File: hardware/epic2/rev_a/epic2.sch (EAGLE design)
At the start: 32 parts, among them J1 PINHD-1X10/0.050, J2 PINHD-1X10/0.050, J3 PINHD-1X10/0.050, U2 FM25LBTDFN-8, U3 CC2538, X1 EPSON-FA-128, X2 FC-12M32.7680KA-A3

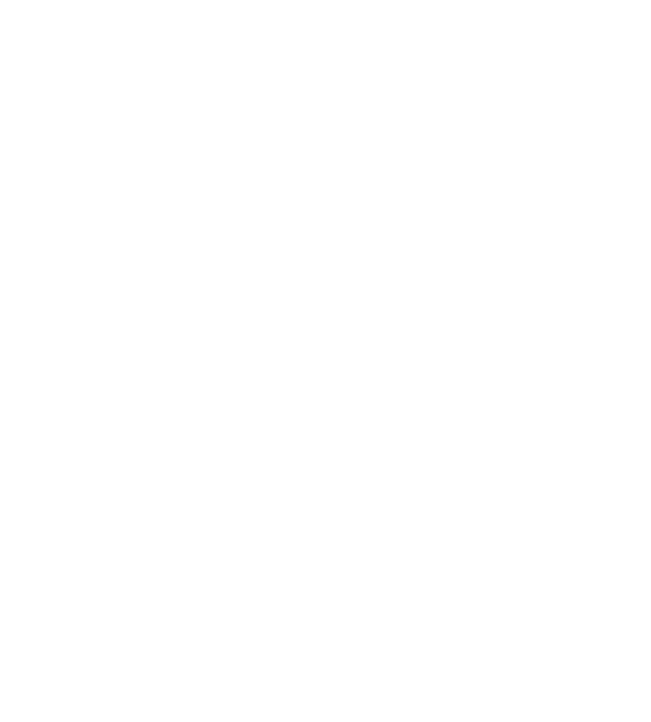
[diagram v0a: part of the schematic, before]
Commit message: new headers
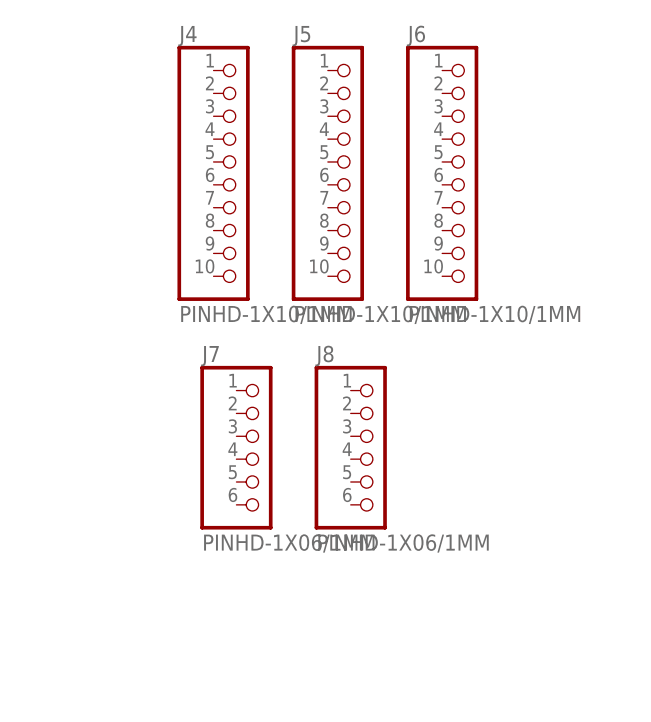
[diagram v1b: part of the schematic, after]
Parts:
- added J4, J5, J6: PINHD-1X10/1MM, headers:PINHD-1X10/1MM
- added J7, J8: PINHD-1X06/1MM, headers:PINHD-1X06/1MM
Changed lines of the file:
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@@
 <part name="C17" library="passives" deviceset="CAPACITOR" device="" value="22pF"/>
 <part name="GND1" library="supply1" deviceset="GND" device=""/>
+<part name="J4" library="headers" deviceset="PINHD-1X10/1MM" device=""/>
+<part name="J5" library="headers" deviceset="PINHD-1X10/1MM" device=""/>
+<part name="J6" library="headers" deviceset="PINHD-1X10/1MM" device=""/>
+<part name="J7" library="headers" deviceset="PINHD-1X06/1MM" device=""/>
+<part name="J8" library="headers" deviceset="PINHD-1X06/1MM" device=""/>
 </parts>
 <sheets>
@@
 <instance part="C17" gate="G$1" x="104.14" y="86.36" rot="R90"/>
 <instance part="GND1" gate="1" x="116.84" y="88.9"/>
+<instance part="J4" gate="G$1" x="264.16" y="170.18"/>
+<instance part="J5" gate="G$1" x="276.86" y="170.18"/>
+<instance part="J6" gate="G$1" x="289.56" y="170.18"/>
+<instance part="J7" gate="G$1" x="266.7" y="137.16"/>
+<instance part="J8" gate="G$1" x="279.4" y="137.16"/>
 </instances>
 <busses>

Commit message: dummy routing for epic2
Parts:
- removed J1, J2, J3: PINHD-1X10/0.050, headers:PINHD-1X10/0.050
- removed J5: PINHD-1X10/1MM, headers:PINHD-1X10/1MM
- removed R5: 4.7k, passives:RESISTOR
- added C18: 10nF, passives:CAPACITOR
- added D1: SML-LX0404SIUPGUSB, leds:SML-LX0404SIUPGUSB
- added R2: 1k, passives:RESISTOR
- added U1: RV-4162-C7, chips:RV-4162-C7
- R3, R4: value 4.7k -> 1k
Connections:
- removed net A3: U3.PA3/ROM-SSI-SEL
- removed net A4: U3.PA4/ROM-SSI-RX
- removed net A5: U3.PA5/ROM-SSI-TX
- removed net A6: U3.PA6
- removed net A7: U3.PA7
- removed net DS2411: U3.PB0
- removed net MISO: U2.SO
- removed net MOSI: U2.SI
- removed net SCK: U2.SCK
- new net !RTC_INT: U1.!INT, U3.PB6/JTAG-TDI
- new net ADC3: J6.4, U3.PA3/ROM-SSI-SEL
- new net ADC4: J6.5, U3.PA4/ROM-SSI-RX
- new net ADC5: J6.6, U3.PA5/ROM-SSI-TX
- new net ADC6: J6.7, U3.PA6
- new net ADC7: J6.8, U3.PA7
- new net B1: J4.10, U3.PB1
- new net B2: J4.9, U3.PB2
- new net B3: J4.8, U3.PB3
- new net B4: J4.7, U3.PB4
- new net DGND_USB: J7.1, U3.DGND_USB
- new net DVDD_USB: J7.4, U3.DVDD_USB
- new net I2C_SCL: J8.2, U1.SCL, U3.PC5
- new net I2C_SDA: J8.3, U1.SDA, U3.PC4
- new net LED_BLUE: R4.2, U3.PC7
- new net LED_GREEN: R3.2, U3.PC6
- new net LED_RED: R2.2, U3.PB0
- new net N$11: D1.G, R3.1
- new net N$12: D1.B, R4.1
- new net N$7: D1.R, R2.1
- new net RTC_CLKOUT: U1.CLKOUT, U3.PB5
- new net SPI_MISO: J7.5, U2.SO, U3.PD0
- new net SPI_MOSI: J7.6, U2.SI, U3.PD1
- new net SPI_SCK: J8.1, U2.SCK, U3.PD2
- new net UNUSED1: J4.2
- new net UNUSED2: J4.3
- new net USB_N: J7.3, U3.USB_N
- new net USB_P: J7.2, U3.USB_P
- net !FRAM_CS: now also U3.PD4; no longer R3.1, U3.PB4
- net !FRAM_HOLD: now also U3.PD3; no longer R4.1, U3.PB3
- net !FRAM_WP: now also U3.PD5; no longer R5.1, U3.PB5
- net !RESET: now also J6.9
- net BOOTLOADER_CTRL: now also J6.3
- net BOOTLOADER_RX: now also J6.1
- net BOOTLOADER_TX: now also J6.2
- net C0: now also J8.6
- net C1: now also J8.5
- net C2: now also J8.4
- net GND: now also C18.2, J6.10, U1.GND
- net TCK: now also J4.5
- net TDO: now also J4.6
- net TMS: now also J4.4
- net VCC: now also C18.1, D1.VDD, J4.1, U1.VCC; no longer R3.2, R4.2, R5.2
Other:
- note added: "I2C address: 0xD0"
- moved on the sheet: C1, C16, C17, C2, C5, J4, J6, J7, J8, R3, R4, U2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

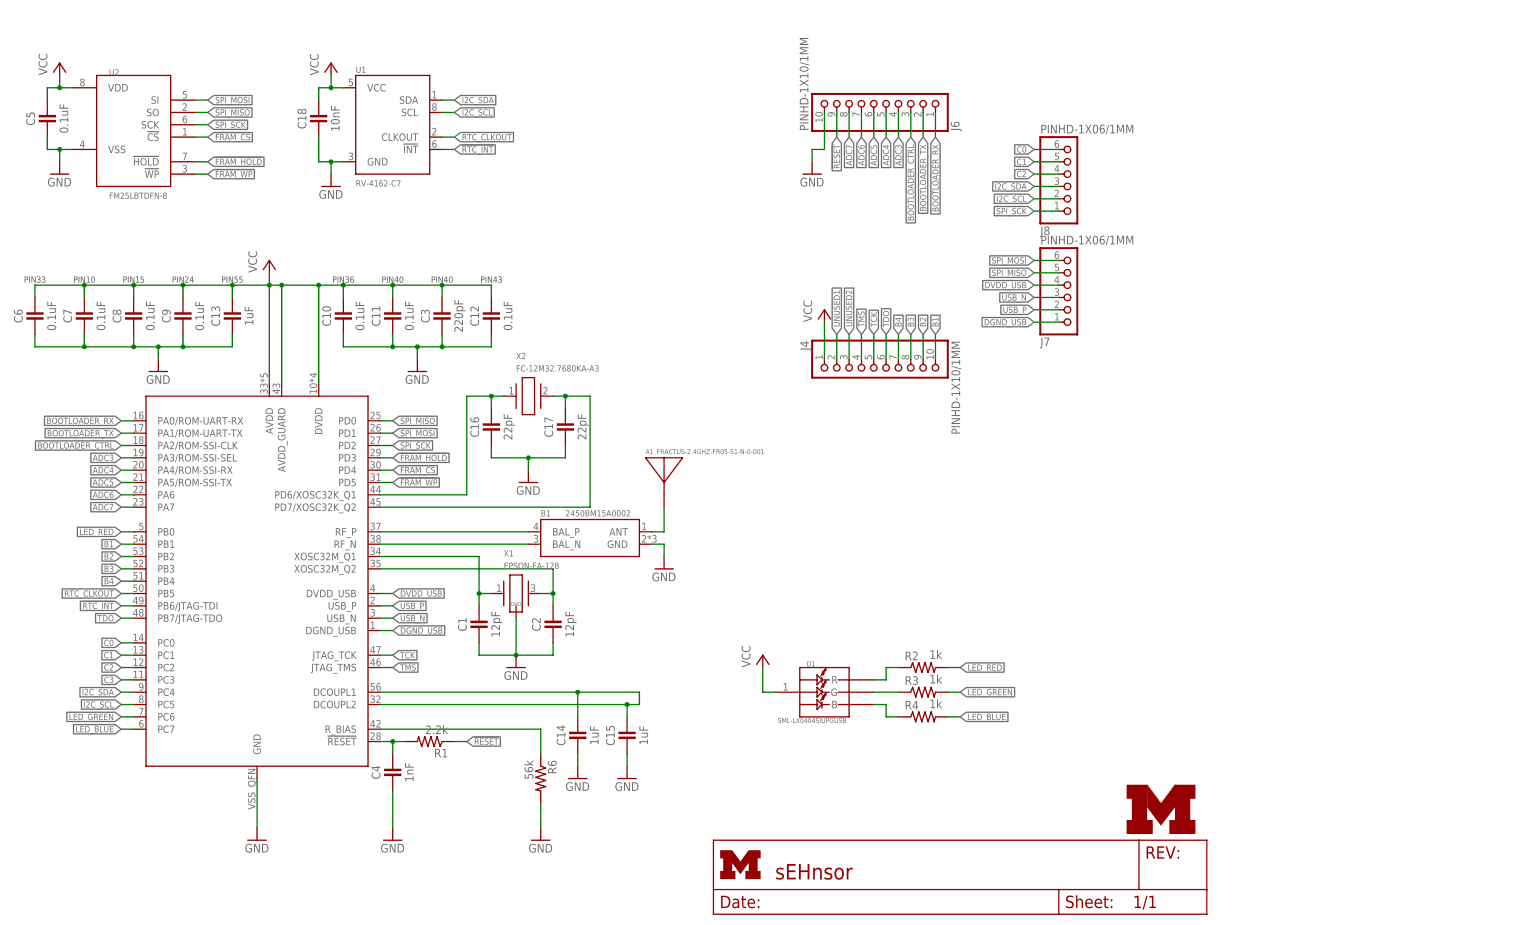
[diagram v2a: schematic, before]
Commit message: rectangular board close to routed
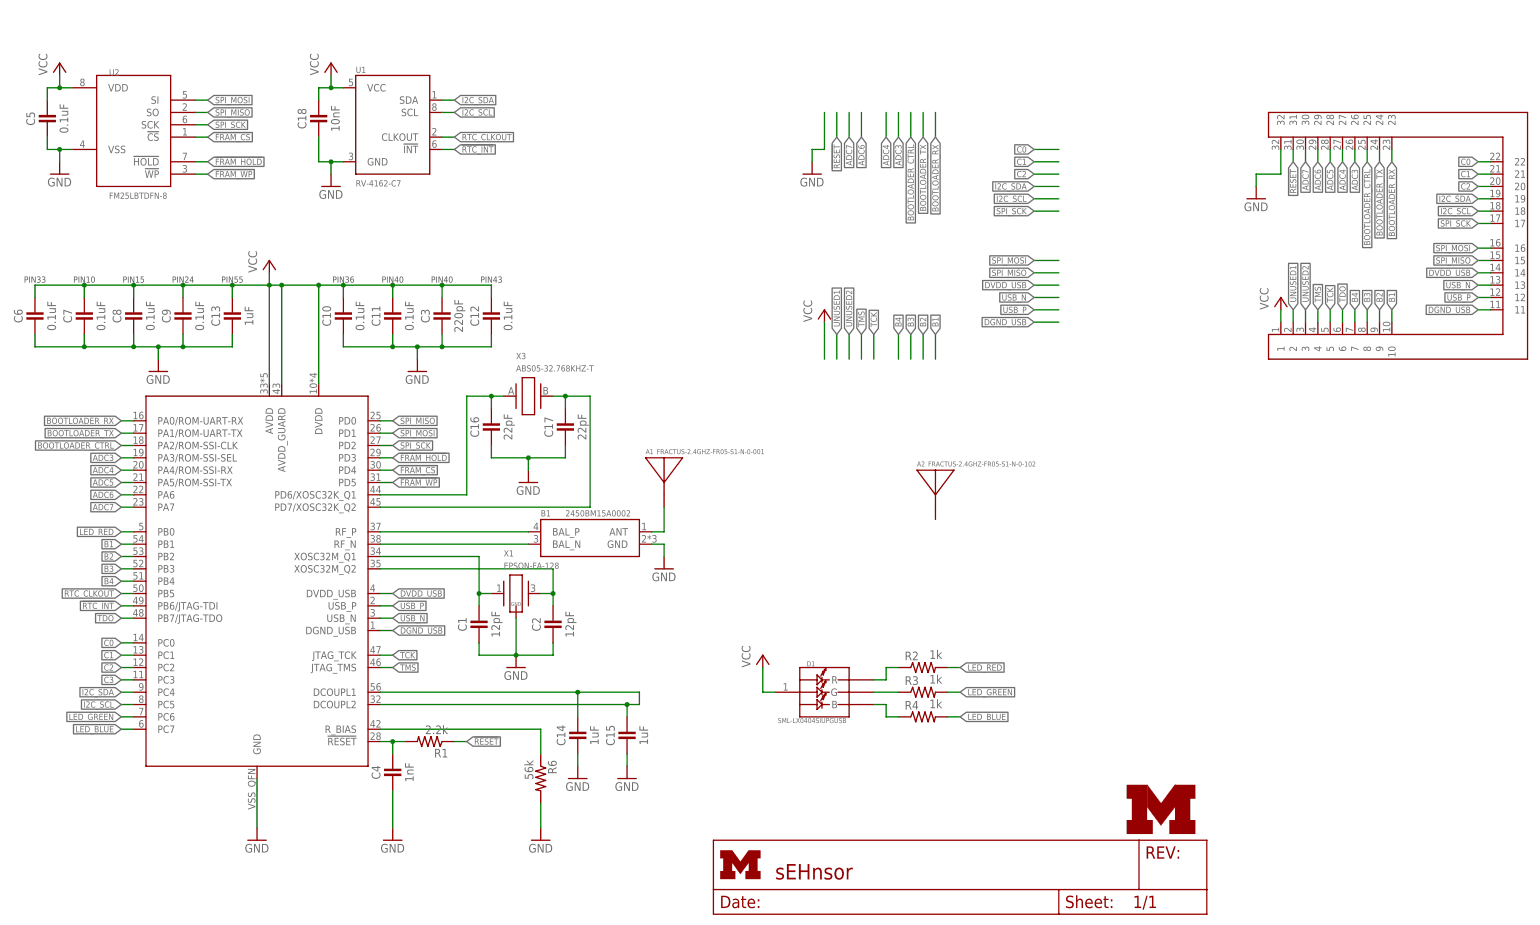
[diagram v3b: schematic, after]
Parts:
- removed J4, J6: PINHD-1X10/1MM, headers:PINHD-1X10/1MM
- removed J7, J8: PINHD-1X06/1MM, headers:PINHD-1X06/1MM
- removed X2: FC-12M32.7680KA-A3, crystals:FC-12M32.7680KA-A3
- added A2: FRACTUS-2.4GHZ-FR05-S1-N-0-102, chips:FRACTUS-2.4GHZ-FR05-S1-N-0-102
- added U$2: EPIC2-HEADER, epic2:EPIC2-HEADER
- added X3: ABS05-32.768KHZ-T, crystals:ABS05-32.768KHZ-T
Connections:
- net !RESET: now also U$2.31; no longer J6.9
- net ADC3: now also U$2.26; no longer J6.4
- net ADC4: now also U$2.27; no longer J6.5
- net ADC5: now also U$2.28; no longer J6.6
- net ADC6: now also U$2.29; no longer J6.7
- net ADC7: now also U$2.30; no longer J6.8
- net B1: now also U$2.10; no longer J4.10
- net B2: now also U$2.9; no longer J4.9
- net B3: now also U$2.8; no longer J4.8
- net B4: now also U$2.7; no longer J4.7
- net BOOTLOADER_CTRL: now also U$2.25; no longer J6.3
- net BOOTLOADER_RX: now also U$2.23; no longer J6.1
- net BOOTLOADER_TX: now also U$2.24; no longer J6.2
- net C0: now also U$2.22; no longer J8.6
- net C1: now also U$2.21; no longer J8.5
- net C2: now also U$2.20; no longer J8.4
- net DGND_USB: now also U$2.11; no longer J7.1
- net DVDD_USB: now also U$2.14; no longer J7.4
- net GND: now also U$2.32; no longer J6.10
- net I2C_SCL: now also U$2.18; no longer J8.2
- net I2C_SDA: now also U$2.19; no longer J8.3
- net N$13: now also X3.2; no longer X2.2
- net N$6: now also X3.1; no longer X2.1
- net SPI_MISO: now also U$2.15; no longer J7.5
- net SPI_MOSI: now also U$2.16; no longer J7.6
- net SPI_SCK: now also U$2.17; no longer J8.1
- net TCK: now also U$2.5; no longer J4.5
- net TDO: now also U$2.6; no longer J4.6
- net TMS: now also U$2.4; no longer J4.4
- net UNUSED1: now also U$2.2; no longer J4.2
- net UNUSED2: now also U$2.3; no longer J4.3
- net USB_N: now also U$2.13; no longer J7.3
- net USB_P: now also U$2.12; no longer J7.2
- net VCC: now also U$2.1; no longer J4.1

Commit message: workin on epic2
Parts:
- removed U$2: EPIC2-HEADER, epic2:EPIC2-HEADER
- added J1: EPIC2-HEADER2, epic2:EPIC2-HEADER2
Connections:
- removed net B1: U$2.10, U3.PB1
- removed net B2: U$2.9, U3.PB2
- removed net UNUSED2: U$2.3
- new net B5: J1.7, U3.PB5
- new net B6: J1.6, U3.PB6/JTAG-TDI
- net !RESET: now also J1.31; no longer U$2.31
- net !RTC_INT: now also U3.PB1; no longer U3.PB6/JTAG-TDI
- net ADC3: now also J1.26; no longer U$2.26
- net ADC4: now also J1.27; no longer U$2.27
- net ADC5: now also J1.28; no longer U$2.28
- net ADC6: now also J1.29; no longer U$2.29
- net ADC7: now also J1.30; no longer U$2.30
- net B3: now also J1.9; no longer U$2.8
- net B4: now also J1.8; no longer U$2.7
- net BOOTLOADER_CTRL: now also J1.25; no longer U$2.25
- net BOOTLOADER_RX: now also J1.23; no longer U$2.23
- net BOOTLOADER_TX: now also J1.24; no longer U$2.24
- net C0: now also J1.22; no longer U$2.22
- net C1: now also J1.21; no longer U$2.21
- net C2: now also J1.20; no longer U$2.20
- net C3: now also J1.19
- net DGND_USB: now also J1.10; no longer U$2.11
- net DVDD_USB: now also J1.13; no longer U$2.14
- net GND: now also J1.32; no longer U$2.32
- net I2C_SCL: now also J1.17; no longer U$2.18
- net I2C_SDA: now also J1.18; no longer U$2.19
- net LED_BLUE: no longer U3.PC7
- net LED_GREEN: no longer U3.PC6
- net LED_RED: no longer U3.PB0
- net RTC_CLKOUT: now also U3.PB2; no longer U3.PB5
- net SPI_MISO: now also J1.14, U3.PB0; no longer U$2.15
- net SPI_MOSI: now also J1.15, U3.PC7; no longer U$2.16
- net SPI_SCK: now also J1.16, U3.PC6; no longer U$2.17
- net TCK: now also J1.4; no longer U$2.5
- net TDO: now also J1.5; no longer U$2.6
- net TMS: now also J1.3; no longer U$2.4
- net UNUSED1: now also J1.2; no longer U$2.2
- net USB_N: now also J1.12; no longer U$2.13
- net USB_P: now also J1.11; no longer U$2.12
- net VCC: now also J1.1; no longer U$2.1

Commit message: getting closer with epic2
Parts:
- removed A1: FRACTUS-2.4GHZ-FR05-S1-N-0-001, chips:FRACTUS-2.4GHZ-FR05-S1-N-0-001
- removed C7: 0.1uF, passives:CAPACITOR
- added C20: 0.1uF, rcl:C-EUC0201
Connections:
- new net UNUSED2: J1.22
- net !FRAM_CS: now also U3.PD1; no longer U3.PD4
- net !FRAM_HOLD: now also U3.PD0; no longer U3.PD3
- net !FRAM_WP: now also U3.PD2; no longer U3.PD5
- net ANTENNA: now also A2.ANTENNA; no longer A1.ANTENNA
- net C0: now also J1.21; no longer J1.22
- net C1: now also J1.20; no longer J1.21
- net C2: now also J1.19; no longer J1.20
- net C3: no longer J1.19
- net GND: now also C20.2; no longer C7.2
- net I2C_SCL: now also U3.PC4; no longer U3.PC5
- net I2C_SDA: now also U3.PC5; no longer U3.PC4
- net LED_BLUE: now also U3.PD4
- net LED_GREEN: now also U3.PD5
- net LED_RED: now also U3.PD3
- net SPI_MISO: no longer U3.PD0
- net SPI_MOSI: no longer U3.PD1
- net SPI_SCK: no longer U3.PD2
- net VCC: now also C20.1; no longer C7.1
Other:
- moved on the sheet: A2

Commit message: no airwaires
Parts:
- removed C18: 10nF, passives:CAPACITOR
- removed U1: RV-4162-C7, chips:RV-4162-C7
- added C7: 10nF, passives:CAPACITOR
- added R5, R7: 10k, passives:RESISTOR
- added U5: RV-3049-C3, chips:RV-3049-C3
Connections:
- removed net RTC_CLKOUT: U1.CLKOUT, U3.PB2
- new net !RTC_CS: U3.PB1, U5.!CS
- new net N$14: R7.2, U5.VBACKUP
- new net N$16: R5.2, U5.CLKOE
- net !RTC_INT: now also U3.PB2, U5.!INT; no longer U1.!INT, U3.PB1
- net GND: now also C7.2, R5.1, R7.1, U5.GND; no longer C18.2, U1.GND
- net I2C_SCL: no longer U1.SCL
- net I2C_SDA: no longer U1.SDA
- net SPI_MISO: now also U5.MISO
- net SPI_MOSI: now also U5.MOSI
- net SPI_SCK: now also U5.SCL
- net VCC: now also C7.1, U5.VCC; no longer C18.1, U1.VCC
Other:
- note removed: "I2C address: 0xD0"
